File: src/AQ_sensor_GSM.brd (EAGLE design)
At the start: 110 x 64 mm, 100 parts, among them IC1 MIC29302WU, IC2 MCP73831/OT, J1 F-1X03-SIP-100-32, J3 PJ-002BH, Q1 MMBT2222, Q2 MMBT2222, Q3 MMBT2222, Q4 MMBT2222, Q5 MMBT2222, Q6 MMBT2222, Q7 MMBT2222, U1 LM7805S/NOPB, U3 TEXAS_INSTRUMENTS_LM1117IMP-3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, U5 TXS0108EPWR, X1 53048-08

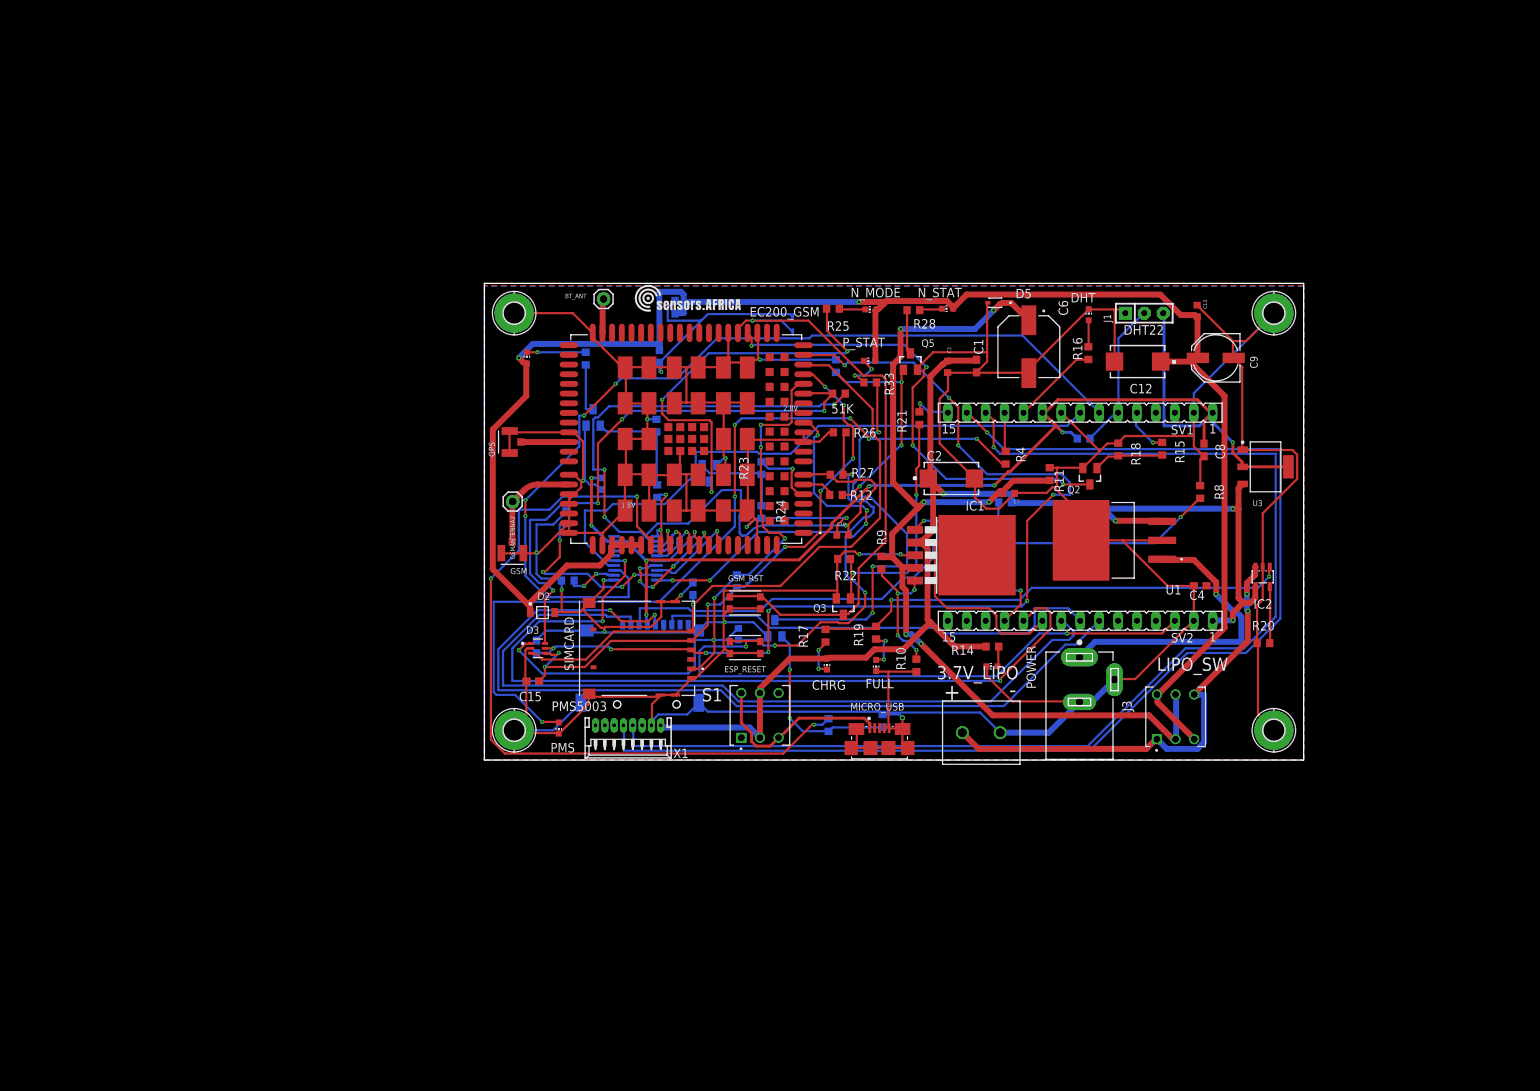
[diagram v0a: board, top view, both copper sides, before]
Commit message: Added Lipo charging system
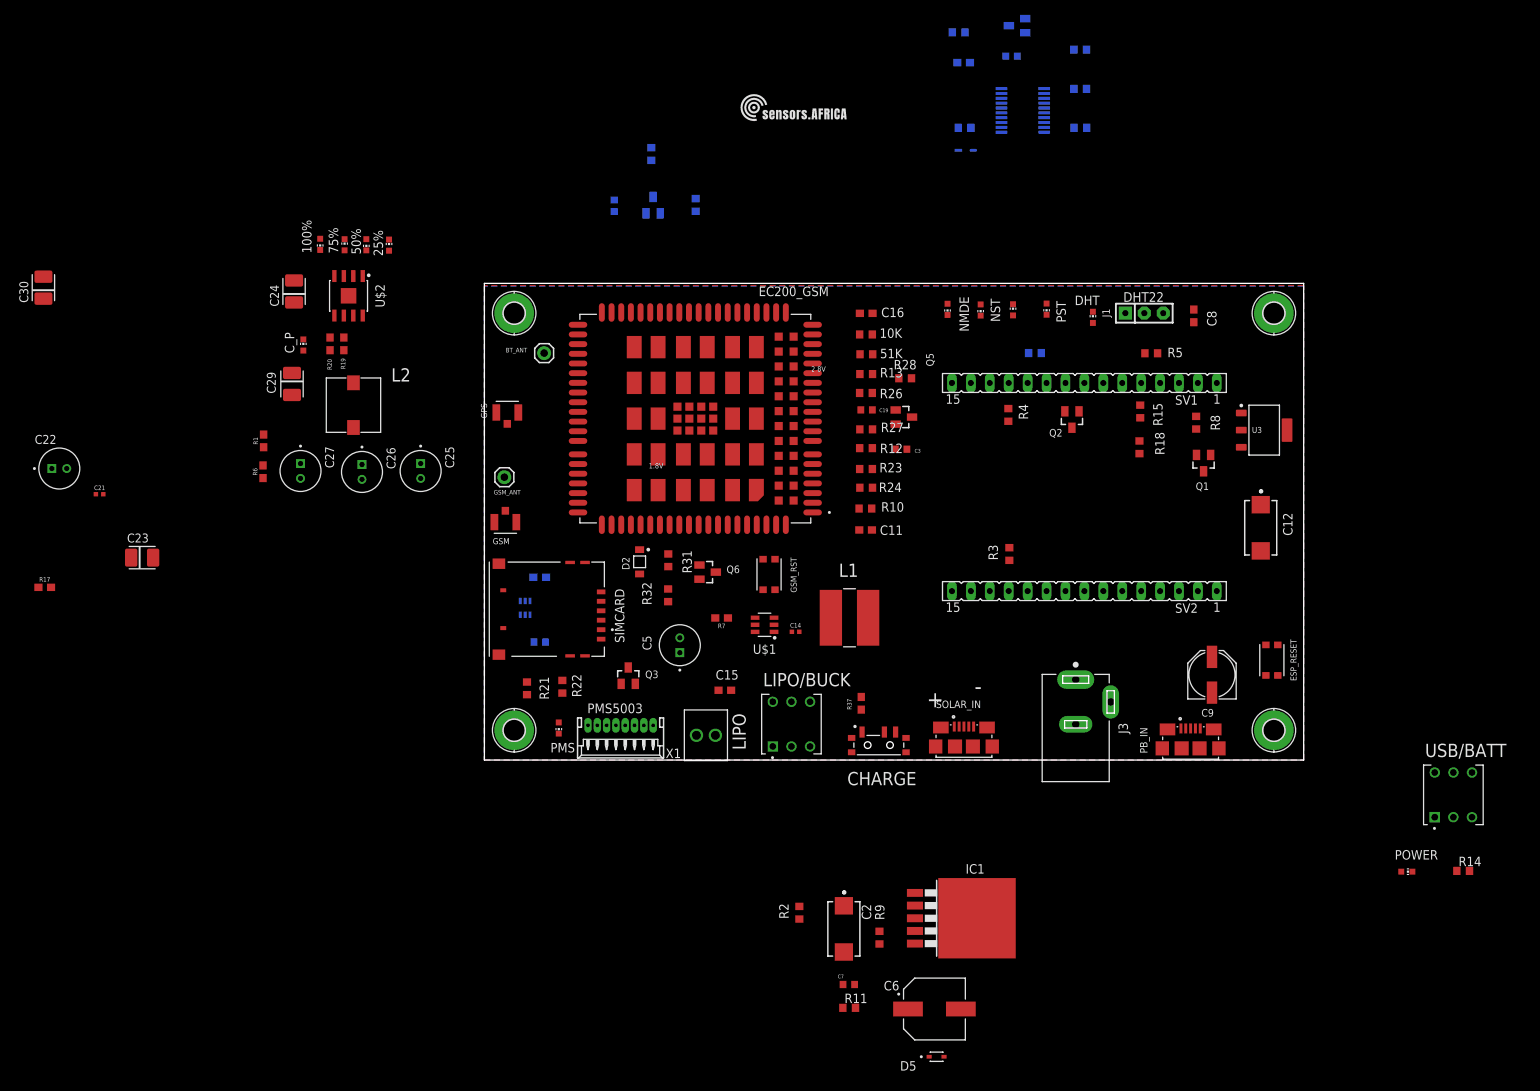
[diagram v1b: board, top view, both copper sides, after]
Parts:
- removed 3.7V_LIPO: 2828XX-2282837-2, Connector:TERMBLK_508-2N
- removed C1, C4: 10uF, rcl:C0603
- removed CHRG: RED, led:CHIP-LED0603
- removed FULL: YELLOW, led:CHIP-LED0603
- removed GSMANTENNA2: (no value), SparkFun-Connectors:1X01
- removed IC2: MCP73831/OT, AQ_sensor_GSM:SOT23-5L
- removed LIPO_SW, S1: TL2285EE, TL2285EE:SW_TL2285EE
- removed MICRO_SD1: TF-01A, TF-01A:TF-01A
- removed MICRO_USB: 10118192-0001LF, AQ_sensor_GSM:AMPHENOL_10118192-0001LF
- removed M_RI, N_MODE, N_STAT, P_STAT: ORANGE, led:CHIP-LED0603
- removed U1: LM7805S/NOPB, LM7805S_NOPB:TO254P1524X483-4N
- added 100%, 25%, 50%, 75%, C_P, MRI, NMDE, NST, PST: ORANGE, led:CHIP-LED0603
- added C14: 22nF, SparkFun-Capacitors:0402-TIGHT
- added C21: 22pF, SparkFun-Capacitors:0402-TIGHT
- added C22, C25, C26, C27, C5: ECA-1HM220, Resistor_Capacitor:CAP_RADIAL_2MM
- added C23, C24, C29, C30: TAJB106K016RNJ, Resistor_Capacitor:CAP_TANT_B
- added CHARGE: PCM12SMTR, AQ_sensor_MRC:SW_PCM12SMTR
- added GSM_ANT: (no value), SparkFun-Connectors:1X01
- added L1: 784787047, Fixed Inductors:784787047
- added L2: 784778010, Fixed Inductors:784778010
- added LIPO: 2828XX-2282834-2, Connector:TERMBLK_254-2N
- added LIPO/BUCK, USB/BATT: TL2285EE, TL2285EE:SW_TL2285EE
- added PB_IN, SOLAR_IN: 10118192-0001LF, AQ_sensor_GSM:AMPHENOL_10118192-0001LF
- added R1: 110k, SparkFun-Resistors:0603
- added R37, R7: 10k, SparkFun-Resistors:0603
- added R6: 15, SparkFun-Resistors:0603
- added U$1: (no value), MT2492:SOT95P280X145-6N
- added U$2: (no value), IP5306:SOIC127P600X165-9T209N
- R17, R19: value 470 -> 2R; device rcl:R0603 -> SparkFun-Resistors:0603
- R20: value 2K -> 220R; device rcl:R0603 -> SparkFun-Resistors:0603
- moved R20 131.6 mm to (-20.7, 55.9), turned to 90 degrees
- moved R17 105.0 mm to (-59.0, 23.2), turned to 0 degrees
- moved D5 101.5 mm to (60.7, -39.8), turned to 0 degrees
- moved C6 89.8 mm to (60.4, -33.4), turned to 0 degrees
- moved R30 86.6 mm to (80.0, 84.9), turned to 180 degrees
- moved R19 81.3 mm to (-18.9, 55.9)
- moved R29 80.8 mm to (64.5, 84.9)
- moved C20 79.6 mm to (70.8, 94.5), turned to 180 degrees
- moved C13 79.5 mm to (17.4, 74.4), flipped to the bottom, turned to 90 degrees
- moved U5 79.5 mm to (72.3, 87.2)
- moved R34 78.4 mm to (80.0, 90.1), turned to 180 degrees
- moved Q7 77.5 mm to (71.5, 98.6), turned to 270 degrees
- moved R11 76.6 mm to (49.0, -33.3), turned to 0 degrees
- moved R35 76.1 mm to (80.0, 95.4), turned to 180 degrees
- moved ESP_RESET 70.7 mm to (105.7, 13.4), turned to 270 degrees
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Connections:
- removed net BP: 3.7V_LIPO.2, IC2.3, LIPO_SW.1, LIPO_SW.6
- removed net CP: C6.1, C7.2, D5.C, IC1.4, LIPO_SW.2, LIPO_SW.5, R11.2, R9.2
- removed net JACKP: J3.1, U1.1
- removed net N$12: FULL.A, R19.1
- removed net N$9: IC2.1, R17.2, R19.2
- removed net USBP: MICRO_USB.1, S1.3, S1.4
- removed net VRTC: C4.1
- new net 3.8V: C6.1, C7.2, D5.C, IC1.4, LIPO/BUCK.1, LIPO/BUCK.6, R11.2, R9.2
- new net 4.2V: C29.1, L2.2, LIPO/BUCK.2, LIPO/BUCK.5, R19.2, U$2.6
- new net 5V_IN: C21.1, C22.1, C30.1, L1.2, R1.2, R17.2, U$2.1
- new net 5V_OUT: C25.1, C26.1, C27.1, U$2.8, USB/BATT.2, USB/BATT.5
- new net BVIN: C5.1, J3.1, R7.2, SOLAR_IN.1, U$1.5
- new net N$10: C21.2, R1.1, R6.2, U$1.3
- new net N$11: R7.1, U$1.4
- new net N$14: 100%.A, 25%.C, 50%.A, 75%.C, U$2.4
- new net N$17: 25%.A, 50%.C, U$2.2
- new net N$18: 100%.C, 75%.A, U$2.3
- new net N$20: CHARGE.1, R37.1
- new net N$21: L2.1, U$2.7
- new net N$24: C24.1, R19.1
- new net N$3: C14.1, U$1.1
- new net N$45: R20.2, R37.2, U$2.5
- new net N$46: C_P.A, R20.1
- new net VUSB: C2.1, C3.2, IC1.2, PB_IN.1, R2.2, USB/BATT.1, USB/BATT.6
- net +3V3: no longer MICRO_SD1.4
- net +5V: now also USB/BATT.3, USB/BATT.4; no longer C1.1, C2.1, C3.2, CHRG.A, IC1.2, IC2.4, R2.2, S1.2, S1.5, U1.3
- net D+: now also PB_IN.3, SOLAR_IN.3; no longer MICRO_USB.3
- net D-: now also PB_IN.2, SOLAR_IN.2; no longer MICRO_USB.2
- net GND: now also C22.2, C23.2, C24.2, C25.2, C26.2, C27.2, C29.2, C30.2, C5.2, CHARGE.2, C_P.C, LIPO.2, PB_IN.4, PB_IN.5, PB_IN.SH1, PB_IN.SH2, PB_IN.SH3, PB_IN.SH4, PB_IN.SH5, PB_IN.SH6, R6.1, SOLAR_IN.4, SOLAR_IN.5, SOLAR_IN.SH1, SOLAR_IN.SH2, SOLAR_IN.SH3, SOLAR_IN.SH4, SOLAR_IN.SH5, SOLAR_IN.SH6, U$1.2, U$2.9; no longer 3.7V_LIPO.1, C1.2, C4.2, FULL.C, IC2.2, MICRO_SD1.6, MICRO_SD1.MP1, MICRO_SD1.MP2, MICRO_SD1.MP3, MICRO_SD1.MP4, MICRO_USB.4, MICRO_USB.5, MICRO_USB.SH1, MICRO_USB.SH2, MICRO_USB.SH3, MICRO_USB.SH4, MICRO_USB.SH5, MICRO_USB.SH6, R20.2, U1.2, U1.4
- net GSM_ANT: now also GSM_ANT.1; no longer GSMANTENNA2.1
- net N$13: now also C23.1, R17.1; no longer IC2.5, R20.1
- net N$30: now also NMDE.C; no longer N_MODE.C
- net N$34: now also NST.C; no longer N_STAT.C
- net N$39: now also PST.C; no longer P_STAT.C
- net N$44: now also MRI.C; no longer M_RI.C
- net N$6: now also C14.2, L1.1, U$1.6; no longer CHRG.C, R17.1
- net TF-CLK: no longer MICRO_SD1.5
- net TF-CS: no longer MICRO_SD1.2
- net TF-MISO: no longer MICRO_SD1.7
- net TF-MOSI: no longer MICRO_SD1.3
- net V_LIPO: now also LIPO.1, LIPO/BUCK.3, LIPO/BUCK.4, MRI.A, NMDE.A, NST.A, PST.A; no longer LIPO_SW.3, LIPO_SW.4, M_RI.A, N_MODE.A, N_STAT.A, P_STAT.A
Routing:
- net GND: track 872.6 -> 0.00 mm, vias 16 -> 0
- net V_LIPO: track 241.5 -> 0.00 mm, vias 2 -> 0
- net +5V: track 177.2 -> 0.00 mm, vias 4 -> 0
- net PMS_TX: track 165.8 -> 0.00 mm, vias 1 -> 0
- net PMS_RX: track 161.5 -> 0.00 mm, vias 1 -> 0
- net +3V3: track 161.4 -> 0.00 mm, vias 8 -> 0
- net SIMRST: track 139.6 -> 0.00 mm, vias 10 -> 0
- net CP: track 135.6 -> 0.00 mm, vias 6 -> 0
- net MCU_TXD: track 123.0 -> 0.00 mm, vias 4 -> 0
- net TF-CLK: track 117.3 -> 0.00 mm, vias 2 -> 0
- net VDD_EXT: track 113.4 -> 0.00 mm, vias 4 -> 0
- net N$4: track 112.1 -> 0.00 mm, vias 6 -> 0
- net MCU_DTR: track 110.8 -> 0.00 mm, vias 3 -> 0
- net TF-CS: track 109.0 -> 0.00 mm
- net PWRSTAT: track 104.4 -> 0.00 mm, vias 3 -> 0
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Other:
- board text removed: "/Users/augustinemwendwa/Downloads/Logo-Files-01 (2) (1) (1).bmp"
- board text removed: "/Users/augustinemwendwa/Downloads/Logo-Files-01 (2) (1).bmp"

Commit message: Reordered components on the PCB, added Lipo charging circuit, added Charging level inidcator LED Bar.
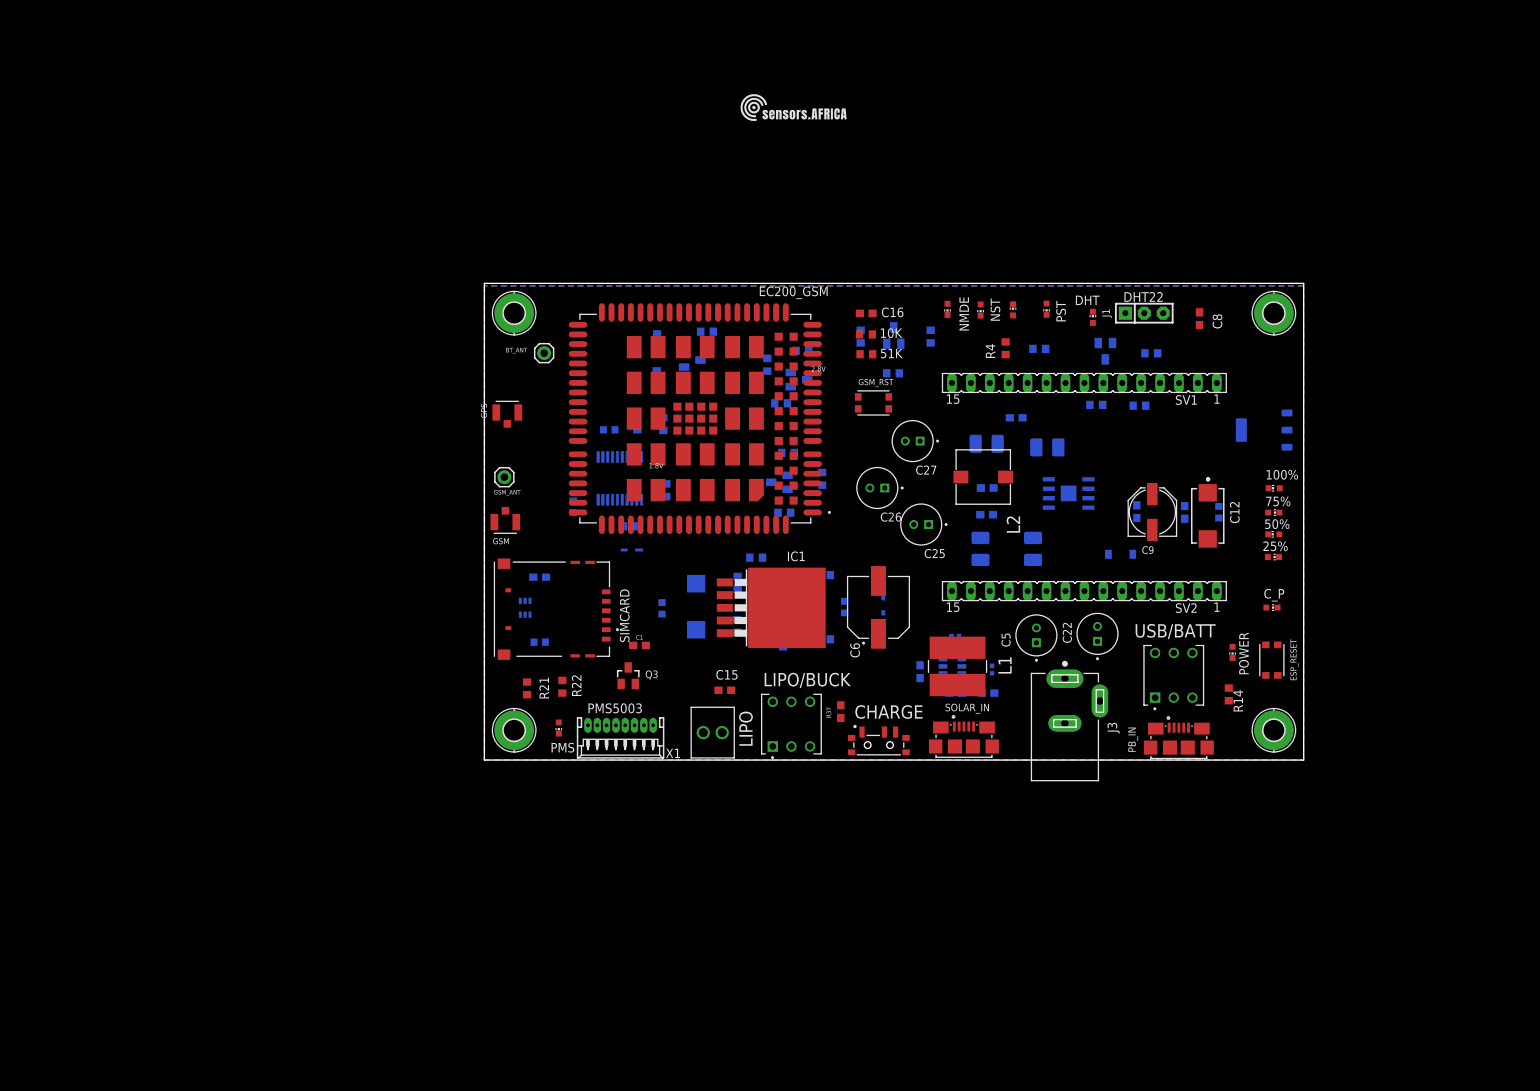
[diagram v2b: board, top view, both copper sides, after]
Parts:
- added C1: 10nF, SparkFun-Capacitors:0603
- moved C22 141.2 mm to (82.3, 16.9), turned to 90 degrees
- moved C30 136.5 mm to (75.6, 42.0), flipped to the bottom, turned to 0 degrees
- moved C_P 134.7 mm to (105.7, 20.5), turned to 270 degrees
- moved R17 132.4 mm to (71.4, 45.9), flipped to the bottom, turned to 180 degrees
- moved 100% 132.2 mm to (106.0, 36.5), turned to 90 degrees
- moved 75% 129.8 mm to (106.0, 33.2), turned to 270 degrees
- moved 50% 127.9 mm to (106.0, 30.3), turned to 90 degrees
- moved 25% 125.9 mm to (105.9, 27.3), turned to 270 degrees
- moved C21 122.1 mm to (68.1, 12.1), flipped to the bottom, turned to 270 degrees
- moved C23 114.4 mm to (67.4, 42.5), flipped to the bottom, turned to 180 degrees
- moved C29 101.9 mm to (73.7, 28.3), flipped to the bottom
- moved R6 101.8 mm to (67.6, 8.99), flipped to the bottom, turned to 0 degrees
- moved U$2 100.3 mm to (78.4, 35.8), flipped to the bottom, turned to 0 degrees
- moved R1 98.9 mm to (63.2, 8.97), flipped to the bottom, turned to 0 degrees
- moved C24 98.4 mm to (66.6, 28.3), flipped to the bottom, turned to 270 degrees
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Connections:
- net GND: now also C1.2, D1.2; no longer D1.1
- net GSM_RST: now also D1.1, GSM_RST.2_1, GSM_RST.2_2
- net PWRKEY: now also C1.1; no longer D1.2, GSM_RST.2_1, GSM_RST.2_2
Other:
- board text removed: "+"
- board text removed: "-"
